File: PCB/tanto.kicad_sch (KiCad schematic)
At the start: 41 parts, among them J1 USB_C, SW1 SW_Push, U1 STM32F072CBT6, U3 XC6206, U4 USBLC6-2SC6

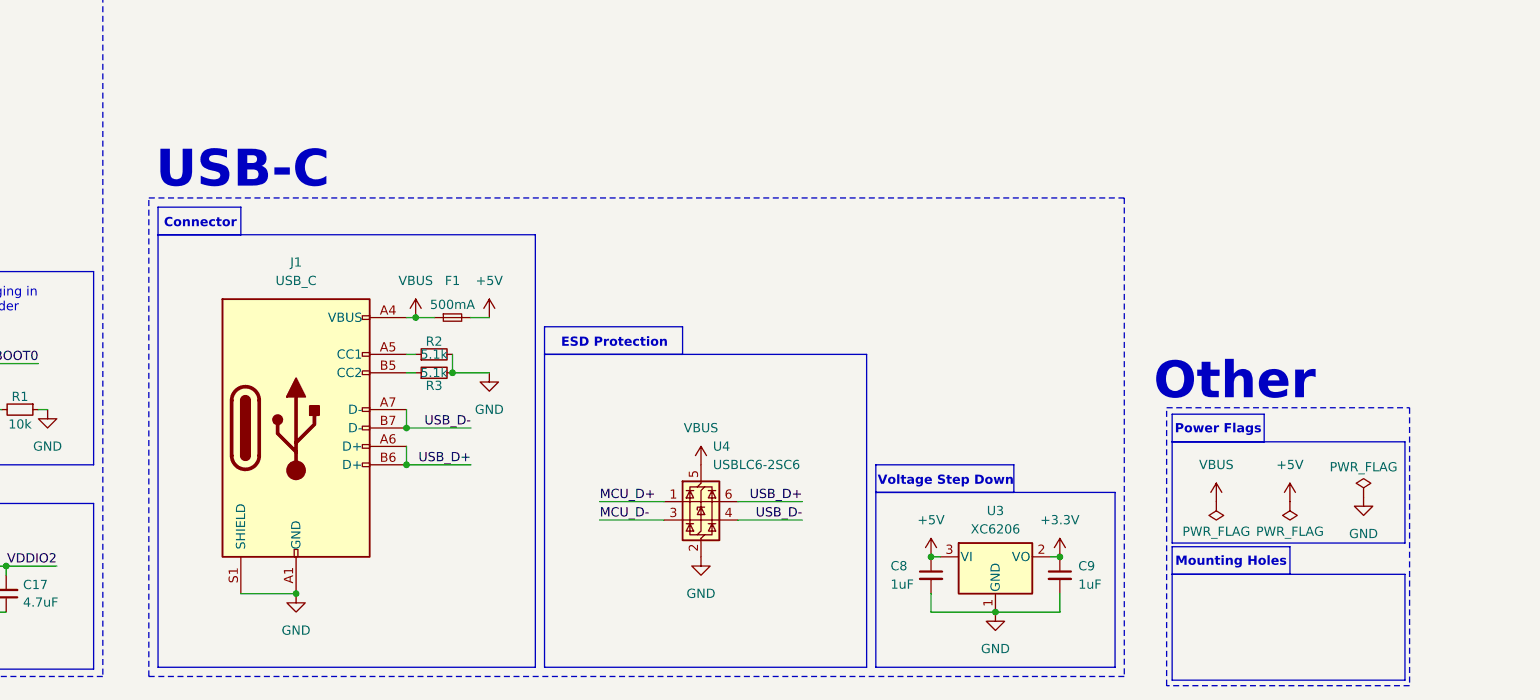
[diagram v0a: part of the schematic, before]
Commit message: PCB and schematic updates
- added jst-sh connector for UDB compatibility
- removed USB input protection
- routed most traces
- arranged all components
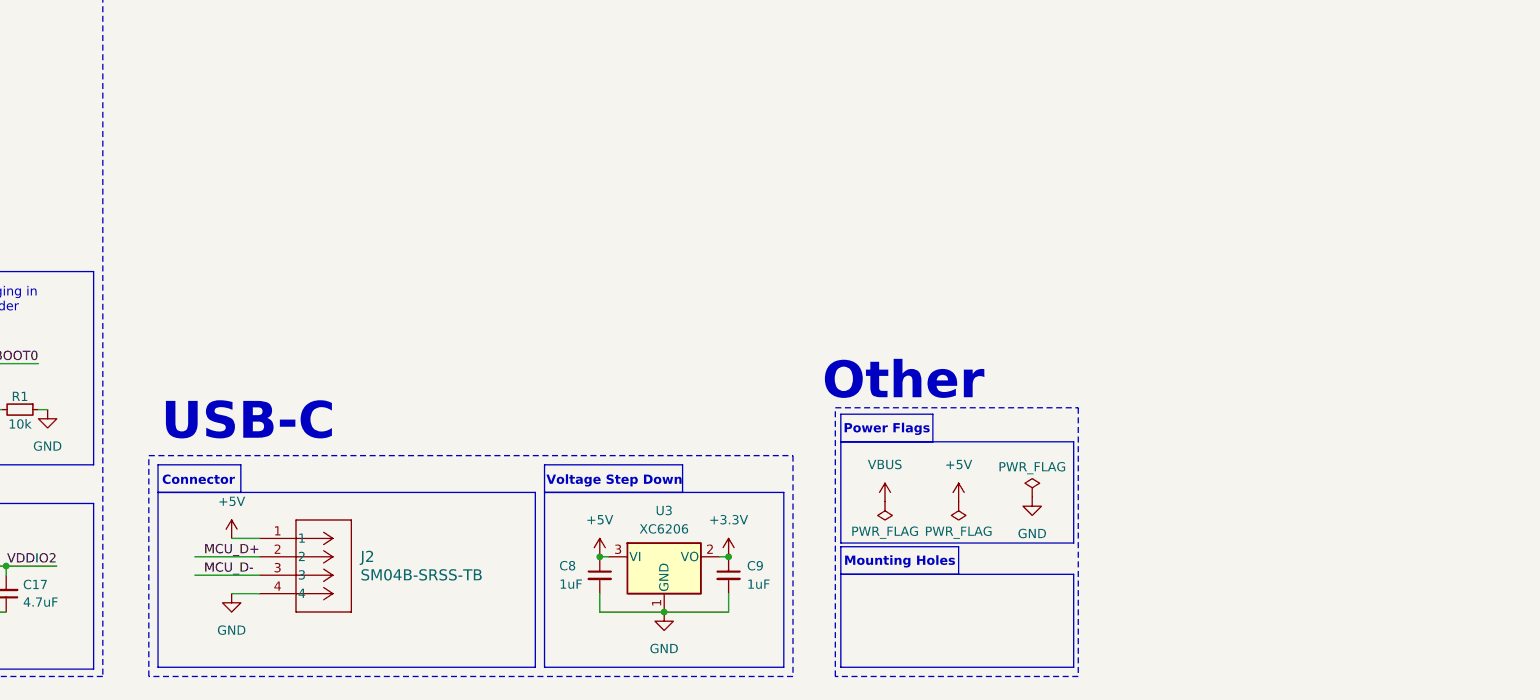
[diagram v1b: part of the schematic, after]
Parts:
- removed F1: 500mA, ScottoKeebs_Components:Fuse_0603, symbol Device:Fuse_Small
- removed J1: USB_C, ScottoKeebs_Components:USB_C_HRO_TYPE-C-31-M-12, symbol Connector:USB_C_Receptacle_USB2.0_14P
- removed R2, R3: 5.1k, ScottoKeebs_Components:Resistor_0402, symbol Device:R_Small
- removed U4: USBLC6-2SC6, ScottoKeebs_Components:ESD_SOT-23-6, symbol Power_Protection:USBLC6-2SC6
- added J2: SM04B-SRSS-TB, CONN_SM04B-SRSS-TB_JST, symbol SM04B-SMSS-TB:SM04B-SRSS-TB
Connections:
- net +5V: now also J2.1
- net GND: now also J2.4
- net MCU_D+: now also J2.2
- net MCU_D-: now also J2.3
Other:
- note removed: "ESD Protection"
- moved on the sheet: C8, C9, U3
